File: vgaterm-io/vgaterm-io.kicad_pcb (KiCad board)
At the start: 2 copper layers, 71.9 x 32.5 mm, 32 parts, among them J1 Conn_01x04, J2 Conn_01x04, J4 DE9_Receptacle, J5 Conn_02x08_Top_Bottom Switch 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, J6 USB_B_Micro Debug, J7 RJ45_LED, J8 Conn_01x10 Data Conn, Q1 Q_Dual_PMOS_S1G1D2S2G2D1, Q2 Q_Dual_PMOS_S1G1D2S2G2D1, Q3 Q_Dual_PMOS_S1G1D2S2G2D1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

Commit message: updating board based on convos with Seth
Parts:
- R11, R12, R15, R16, R7, R8: value 20k -> 40k
- R3, R4: value 20k -> 300k
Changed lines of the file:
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@@
         (effects (font (size 1 1) (thickness 0.15)))
     )
-    (fp_text value "20k" (at 0 1.65) (layer "F.Fab")
+    (fp_text value "40k" (at 0 1.65) (layer "F.Fab")
         (effects (font (size 1 1) (thickness 0.15)))
     )
@@
         (effects (font (size 1 1) (thickness 0.15)))
     )
-    (fp_text value "20k" (at 0 1.65) (layer "F.Fab")
+    (fp_text value "40k" (at 0 1.65) (layer "F.Fab")
         (effects (font (size 1 1) (thickness 0.15)))
     )
@@
         (effects (font (size 1 1) (thickness 0.15)))
     )
-    (fp_text value "20k" (at 0 1.65) (layer "F.Fab")
+    (fp_text value "40k" (at 0 1.65) (layer "F.Fab")
         (effects (font (size 1 1) (thickness 0.15)))
     )
@@
         (effects (font (size 1 1) (thickness 0.15)))
     )
-    (fp_text value "20k" (at 0 1.65 90) (layer "F.Fab")
+    (fp_text value "40k" (at 0 1.65 90) (layer "F.Fab")
         (effects (font (size 1 1) (thickness 0.15)))
     )
@@
         (effects (font (size 1 1) (thickness 0.15)))
     )
-    (fp_text value "20k" (at 0 1.65) (layer "F.Fab")
+    (fp_text value "40k" (at 0 1.65) (layer "F.Fab")
         (effects (font (size 1 1) (thickness 0.15)))
     )
@@
         (effects (font (size 1 1) (thickness 0.15)) (justify mirror))
     )
-    (fp_text value "20k" (at 0 -1.65 -360) (layer "B.Fab")
+    (fp_text value "300k" (at 0 -1.65 -360) (layer "B.Fab")
         (effects (font (size 1 1) (thickness 0.15)) (justify mirror))
     )
@@
         (effects (font (size 1 1) (thickness 0.15)) (justify mirror))
     )
-    (fp_text value "20k" (at 0 -1.65) (layer "B.Fab")
+    (fp_text value "300k" (at 0 -1.65) (layer "B.Fab")
         (effects (font (size 1 1) (thickness 0.15)) (justify mirror))
     )
@@
         (effects (font (size 1 1) (thickness 0.15)) (justify mirror))
     )
-    (fp_text value "20k" (at 0 -1.65) (layer "B.Fab")
+    (fp_text value "40k" (at 0 -1.65) (layer "B.Fab")
         (effects (font (size 1 1) (thickness 0.15)) (justify mirror))
     )

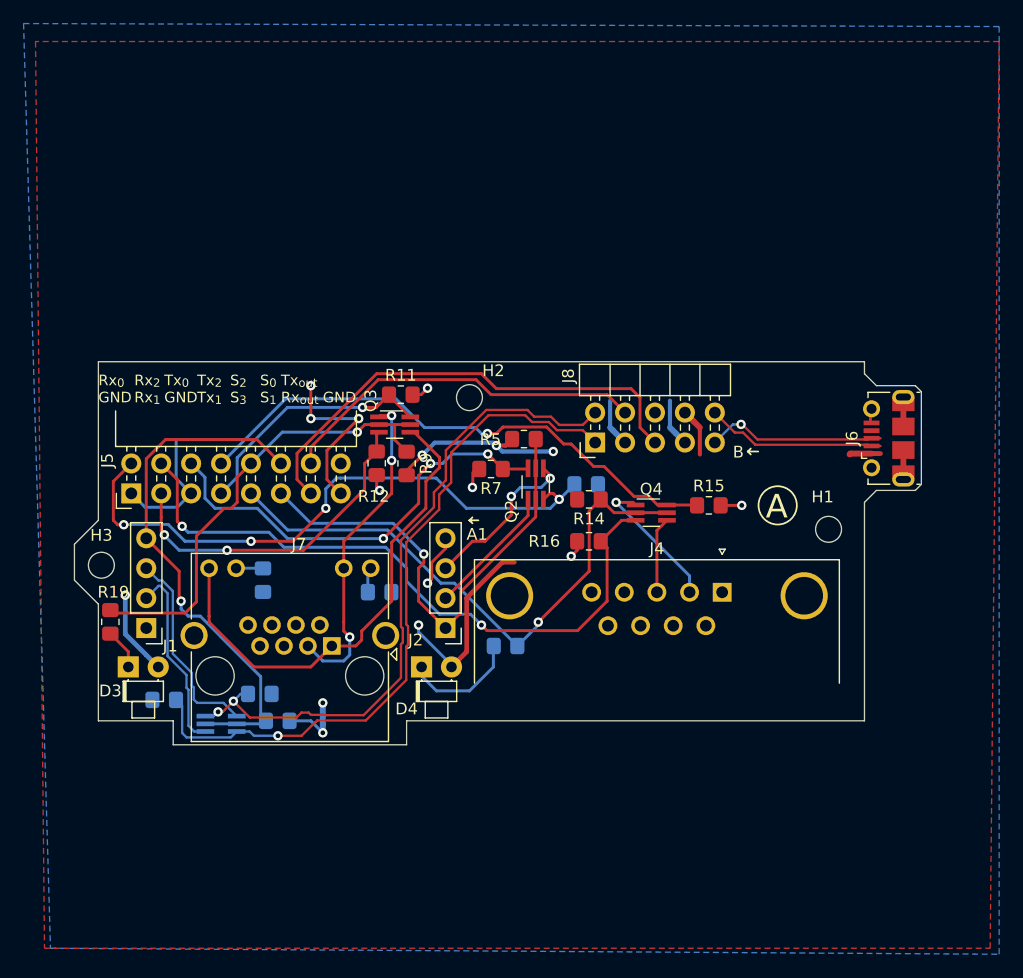
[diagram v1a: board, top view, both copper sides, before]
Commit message: updating timing board hsync vsync delay
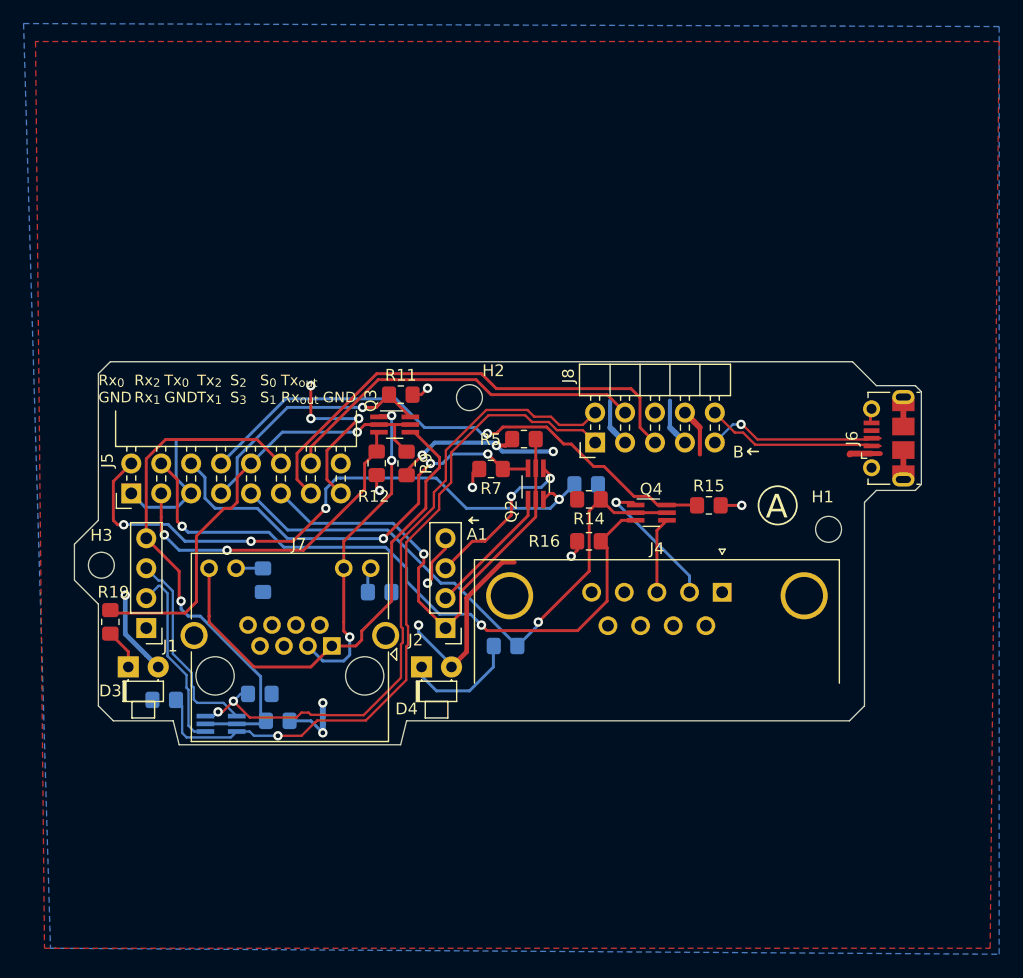
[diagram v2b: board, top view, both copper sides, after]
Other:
- outline, holes or cut-outs redrawn
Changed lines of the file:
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@@
     (property "ki_keywords" "transistor PMOS P-MOS P-MOSFET")
     (attr smd)
-    (fp_text reference "Q1" (at -3.048 1.015) (layer "B.SilkS")
+    (fp_text reference "Q1" (at -1.778 -1.525) (layer "B.SilkS")
         (effects (font (size 0.8 0.9) (thickness 0.15)) (justify mirror))
     )
@@
   (gr_line (start 88.138 63.246) (end 88.392 63.5)
     (stroke (width 0.15) (type default)) (layer "F.SilkS"))
+  (gr_line (start 56.642 50.8) (end 57.658 49.784)
+    (stroke (width 0.1) (type default)) (layer "Edge.Cuts"))
   (gr_line (start 126.492 60.198) (end 125.984 60.706)
     (stroke (width 0.1) (type default)) (layer "Edge.Cuts"))
   (gr_line (start 126.492 60.198) (end 126.492 52.324)
     (stroke (width 0.1) (type default)) (layer "Edge.Cuts"))
-  (gr_line (start 122.682 51.816) (end 121.666 50.8)
-    (stroke (width 0.1) (type default)) (layer "Edge.Cuts"))
-  (gr_line (start 56.642 49.784) (end 56.642 63.246)
+  (gr_line (start 56.642 50.8) (end 56.642 63.246)
     (stroke (width 0.1) (type default)) (layer "Edge.Cuts"))
   (gr_line (start 54.61 65.278) (end 56.642 63.246)
     (stroke (width 0.1) (type default)) (layer "Edge.Cuts"))
-  (gr_line (start 121.666 80.264) (end 121.666 61.722)
+  (gr_line (start 121.666 78.994) (end 121.666 61.722)
     (stroke (width 0.1) (type default)) (layer "Edge.Cuts"))
   (gr_line (start 54.61 68.326) (end 56.642 70.358)
     (stroke (width 0.1) (type default)) (layer "Edge.Cuts"))
-  (gr_line (start 121.666 50.8) (end 121.666 49.784)
-    (stroke (width 0.1) (type default)) (layer "Edge.Cuts"))
-  (gr_line (start 56.642 80.264) (end 56.642 70.358)
+  (gr_line (start 56.642 78.994) (end 56.642 70.358)
     (stroke (width 0.1) (type default)) (layer "Edge.Cuts"))
   (gr_line (start 54.61 68.326) (end 54.61 65.278)
     (stroke (width 0.1) (type default)) (layer "Edge.Cuts"))
-  (gr_line (start 62.992 80.264) (end 56.642 80.264)
+  (gr_line (start 62.992 80.264) (end 57.912 80.264)
     (stroke (width 0.1) (type default)) (layer "Edge.Cuts"))
-  (gr_line (start 82.804 80.264) (end 82.804 82.296)
+  (gr_line (start 57.912 80.264) (end 56.642 78.994)
+    (stroke (width 0.1) (type default)) (layer "Edge.Cuts"))
+  (gr_line (start 82.804 80.264) (end 82.296 82.296)
+    (stroke (width 0.1) (type default)) (layer "Edge.Cuts"))
+  (gr_line (start 120.65 49.784) (end 122.682 51.816)
     (stroke (width 0.1) (type default)) (layer "Edge.Cuts"))
   (gr_line (start 126.492 52.324) (end 125.984 51.816)
@@
   (gr_line (start 125.984 60.706) (end 122.682 60.706)
     (stroke (width 0.1) (type default)) (layer "Edge.Cuts"))
-  (gr_line (start 121.666 49.784) (end 56.642 49.784)
+  (gr_line (start 120.65 49.784) (end 57.658 49.784)
     (stroke (width 0.1) (type default)) (layer "Edge.Cuts"))
-  (gr_line (start 62.992 82.296) (end 62.992 80.264)
+  (gr_line (start 63.5 82.296) (end 62.992 80.264)
     (stroke (width 0.1) (type default)) (layer "Edge.Cuts"))
   (gr_line (start 122.682 60.706) (end 121.666 61.722)
     (stroke (width 0.1) (type default)) (layer "Edge.Cuts"))
-  (gr_line (start 82.804 80.264) (end 121.666 80.264)
+  (gr_line (start 82.804 80.264) (end 120.396 80.264)
     (stroke (width 0.1) (type default)) (layer "Edge.Cuts"))
-  (gr_line (start 82.804 82.296) (end 62.992 82.296)
+  (gr_line (start 82.296 82.296) (end 63.5 82.296)
     (stroke (width 0.1) (type default)) (layer "Edge.Cuts"))
   (gr_line (start 125.984 51.816) (end 122.682 51.816)
     (stroke (width 0.1) (type default)) (layer "Edge.Cuts"))
+  (gr_line (start 120.396 80.264) (end 121.666 78.994)
+    (stroke (width 0.1) (type default)) (layer "Edge.Cuts"))
   (gr_text "Rx_{0}\nGND" (at 56.642 53.34) (layer "F.SilkS")

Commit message: board updates and adding vga breakout
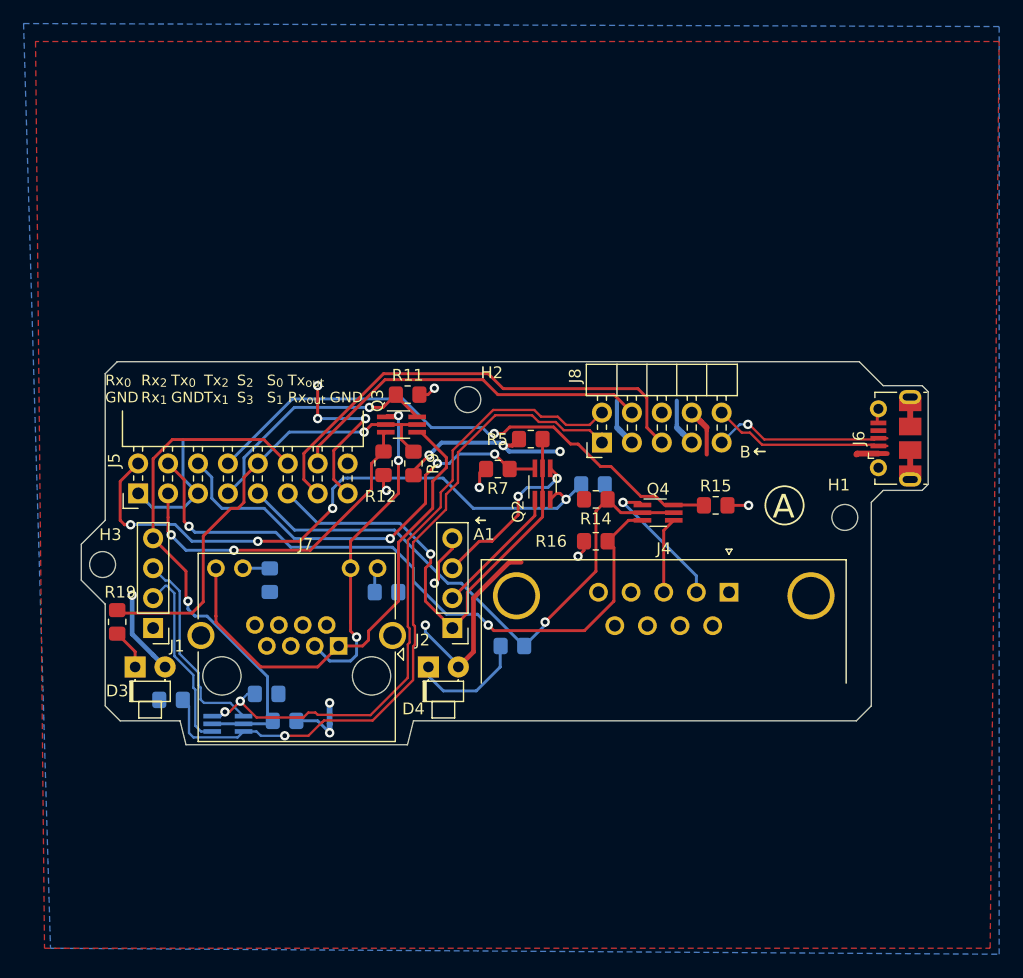
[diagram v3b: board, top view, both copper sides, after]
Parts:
- moved H1 1.71 mm to (120.0, 63.0)
- moved J2 0.58 mm to (86.7, 72.4)
- moved Q2 0.58 mm to (94.3, 60.2)
- moved R5 0.58 mm to (93.3, 56.3)
- moved R3 0.58 mm to (62.8, 78.5)
- moved D3 0.58 mm to (59.8, 75.7)
- moved D4 0.58 mm to (84.7, 75.7)
- moved J1 0.58 mm to (61.3, 72.4)
- moved J4 0.58 mm to (110.2, 69.3)
- moved J5 0.58 mm to (60.0, 61.0)
- moved J6 0.58 mm to (124.3, 56.3)
- moved J7 0.58 mm to (77.0, 73.9)
- moved J8 0.58 mm to (99.4, 56.6)
- moved Q1 0.58 mm to (67.6, 80.5)
- moved Q3 0.58 mm to (82.4, 55.1)
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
